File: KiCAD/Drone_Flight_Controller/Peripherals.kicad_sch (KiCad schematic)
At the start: 57 parts, among them J1 XT60, J2 0.5mΩ high side shunt, Q1 2N2222A, U1 74AHC1G125, U2 74AHC1G125, U3 74AHC1G125, U4 74AHC1G125, U9 INA195

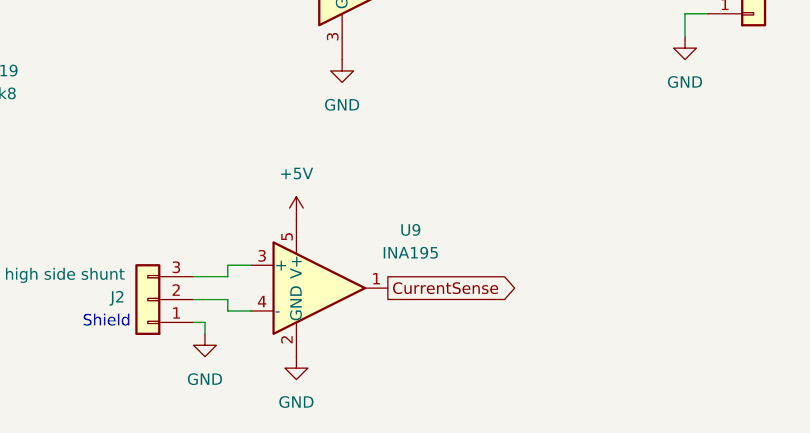
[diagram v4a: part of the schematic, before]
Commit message: Add resistor parallel to shunt to lower EMI
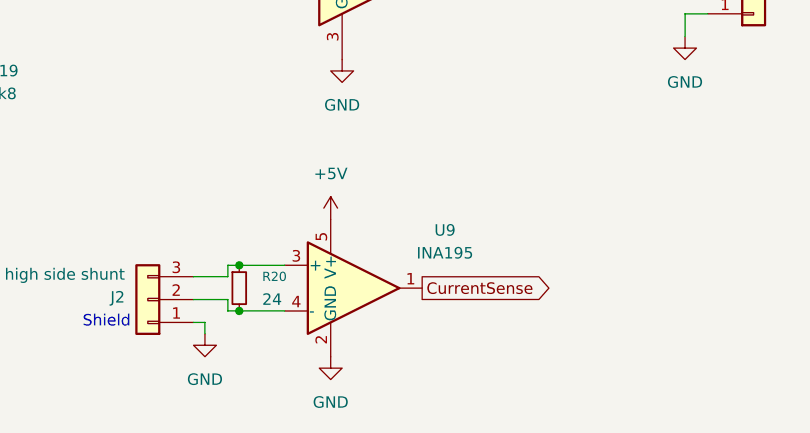
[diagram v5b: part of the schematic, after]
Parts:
- added R20: 24, Resistor_SMD:R_0805_2012Metric_Pad1.20x1.40mm_HandSolder, symbol Device:R_Small
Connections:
- net at J2.3 (Pin_3), U9.3 (+): now also R20.1
- net at J2.2 (Pin_2), U9.4 (-): now also R20.2
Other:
- moved on the sheet: U9
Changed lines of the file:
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@@
 	)
 	(junction
+		(at 130.81 184.15)
+		(diameter 0)
+		(color 0 0 0 0)
+	)
+	(junction
 		(at 91.44 172.72)
 		(diameter 0)
@@
 	)
 	(junction
+		(at 130.81 179.07)
+		(diameter 0)
+		(color 0 0 0 0)
+	)
+	(junction
 		(at 38.1 116.84)
 		(diameter 0)
@@
 	(wire
 		(pts
-			(xy 129.54 179.07) (xy 132.08 179.07)
+			(xy 129.54 179.07) (xy 130.81 179.07)
 		)
 		(stroke
@@
 	(wire
 		(pts
+			(xy 130.81 184.15) (xy 135.89 184.15)
+		)
+		(stroke
+			(width 0)
+			(type default)
+		)
+	)
+	(wire
+		(pts
 			(xy 180.34 113.03) (xy 182.88 113.03)
 		)
@@
 	(wire
 		(pts
+			(xy 130.81 179.07) (xy 135.89 179.07)
+		)
+		(stroke
+			(width 0)
+			(type default)
+		)
+	)
+	(wire
+		(pts
 			(xy 45.72 69.85) (xy 45.72 72.39)
 		)
@@
 		)
 	)
-	(wire
-		(pts
-			(xy 132.08 184.15) (xy 129.54 184.15)
-		)
-		(stroke
-			(width 0)
-			(type default)
-		)
-	)
 	(bus
 		(pts
@@
 		)
 	)
+	(wire
+		(pts
+			(xy 129.54 184.15) (xy 130.81 184.15)
+		)
+		(stroke
+			(width 0)
+			(type default)
+		)
+	)
 	(bus
 		(pts
@@
 	(global_label "CurrentSense"
 		(shape output)
-		(at 147.32 181.61 0)
+		(at 151.13 181.61 0)
 		(fields_autoplaced yes)
 		(effects
@@
 		)
 		(property "Intersheetrefs" "${INTERSHEET_REFS}"
-			(at 162.8237 181.61 0)
+			(at 166.6337 181.61 0)
 			(effects
 				(font
@@
 	(symbol
 		(lib_id "Amplifier_Current:INA195")
-		(at 139.7 181.61 0)
+		(at 143.51 181.61 0)
 		(unit 1)
 		(exclude_from_sim no)
@@
 		(fields_autoplaced yes)
 		(property "Reference" "U9"
-			(at 149.86 175.1898 0)
+			(at 153.67 175.1898 0)
 			(effects
 				(font
@@
 		)
 		(property "Value" "INA195"
-			(at 149.86 177.7298 0)
+			(at 153.67 177.7298 0)
 			(effects
 				(font
@@
 		)
 		(property "Footprint" "Package_TO_SOT_SMD:SOT-23-5"
-			(at 139.7 181.61 0)
+			(at 143.51 181.61 0)
 			(effects
 				(font
@@
 		)
 		(property "Datasheet" "http://www.ti.com/lit/ds/symlink/ina193.pdf"
-			(at 139.7 181.61 0)
+			(at 143.51 181.61 0)
 			(effects
 				(font
@@
 		)
 		(property "Description" "Current Shunt Monitor −16V to +80V Common-Mode Range, 100V/V, SOT-23-5"
-			(at 139.7 181.61 0)
+			(at 143.51 181.61 0)
 			(effects
 				(font
@@
 	(symbol
 		(lib_id "power:+5V")
-		(at 137.16 173.99 0)
+		(at 140.97 173.99 0)
 		(unit 1)
 		(exclude_from_sim no)
@@
 		(fields_autoplaced yes)
 		(property "Reference" "#PWR060"
-			(at 137.16 177.8 0)
+			(at 140.97 177.8 0)
 			(effects
 				(font
@@
 		)
 		(property "Value" "+5V"
-			(at 137.16 168.91 0)
+			(at 140.97 168.91 0)
 			(effects
 				(font
@@
 		)
 		(property "Footprint" ""
-			(at 137.16 173.99 0)
+			(at 140.97 173.99 0)
 			(effects
 				(font
@@
 		)
 		(property "Datasheet" ""
-			(at 137.16 173.99 0)
+			(at 140.97 173.99 0)
 			(effects
 				(font
@@
 		)
 		(property "Description" "Power symbol creates a global label with name \"+5V\""
-			(at 137.16 173.99 0)
+			(at 140.97 173.99 0)
 			(effects
 				(font
@@
 	(symbol
 		(lib_id "power:GND")
-		(at 137.16 189.23 0)
+		(at 140.97 189.23 0)
 		(unit 1)
 		(exclude_from_sim no)
@@
 		(fields_autoplaced yes)
 		(property "Reference" "#PWR061"
-			(at 137.16 195.58 0)
+			(at 140.97 195.58 0)
 			(effects
 				(font
@@
 		)
 		(property "Value" "GND"
-			(at 137.16 194.31 0)
+			(at 140.97 194.31 0)
 			(effects
 				(font
@@
 		)
 		(property "Footprint" ""
-			(at 137.16 189.23 0)
+			(at 140.97 189.23 0)
 			(effects
 				(font
@@
 		)
 		(property "Datasheet" ""
-			(at 137.16 189.23 0)
+			(at 140.97 189.23 0)
 			(effects
 				(font
@@
 		)
 		(property "Description" "Power symbol creates a global label with name \"GND\" , ground"
-			(at 137.16 189.23 0)
+			(at 140.97 189.23 0)
 			(effects
 				(font
@@
 					(unit 1)
 				)
+			)
+		)
+	)
+	(symbol
+		(lib_id "Device:R_Small")
+		(at 130.81 181.61 0)
+		(unit 1)
+		(exclude_from_sim no)
+		(in_bom yes)
+		(on_board yes)
+		(dnp no)
+		(fields_autoplaced yes)
+		(property "Reference" "R20"
+			(at 133.35 180.3399 0)
+			(effects
+				(font
+					(size 1.016 1.016)
+				)
+				(justify left)
+			)
+		)
+		(property "Value" "24"
+			(at 133.35 182.8799 0)
+			(effects
+				(font
+					(size 1.27 1.27)
+				)
+				(justify left)
+			)
+		)
+		(property "Footprint" "Resistor_SMD:R_0805_2012Metric_Pad1.20x1.40mm_HandSolder"
+			(at 130.81 181.61 0)
+			(effects
+				(font
+					(size 1.27 1.27)
+				)
+				(hide yes)
+			)
+		)
+		(property "Datasheet" "~"
+			(at 130.81 181.61 0)
+			(effects
+				(font
+					(size 1.27 1.27)
+				)
+				(hide yes)
+			)
+		)
+		(property "Description" "Resistor, small symbol"
+			(at 130.81 181.61 0)
+			(effects
+				(font
+					(size 1.27 1.27)
+				)
+				(hide yes)
+			)
+		)
+		(pin "2"
+		)
+		(pin "1"
+		)
+		(instances
+			(project ""
+				(path "/51ab9491-7068-4b24-bb38-47a0c739796e/a1832adb-c070-4778-a5ef-97ea378c06da"
+					(reference "R20")
+					(unit 1)
+				)
